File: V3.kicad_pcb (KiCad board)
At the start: 2 copper layers, 128.2 x 61 mm, 109 parts, among them IC1 TPS62840DLCR","TPS62840DLCR, J1 Conn_01x04, J2 Conn_01x04, J3 FFC2B28-24-G, J4 Conn_01x04, J6 Conn_01x02, J7 Conn_01x02, Q3 FDN304P","FDN304P, Q4 FDN304P","FDN304P, Q8 SI1308EDL","SI1308EDL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

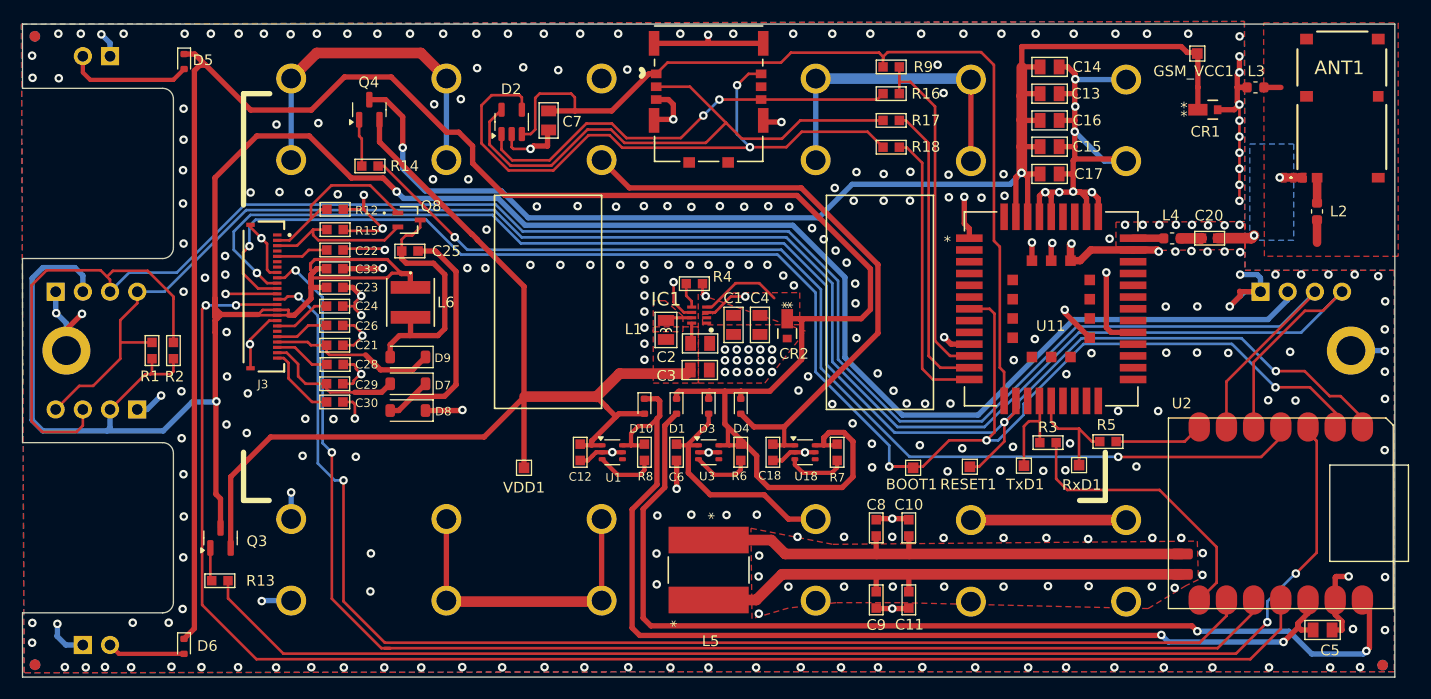
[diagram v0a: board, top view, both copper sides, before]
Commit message: edit fotprint of xiao module
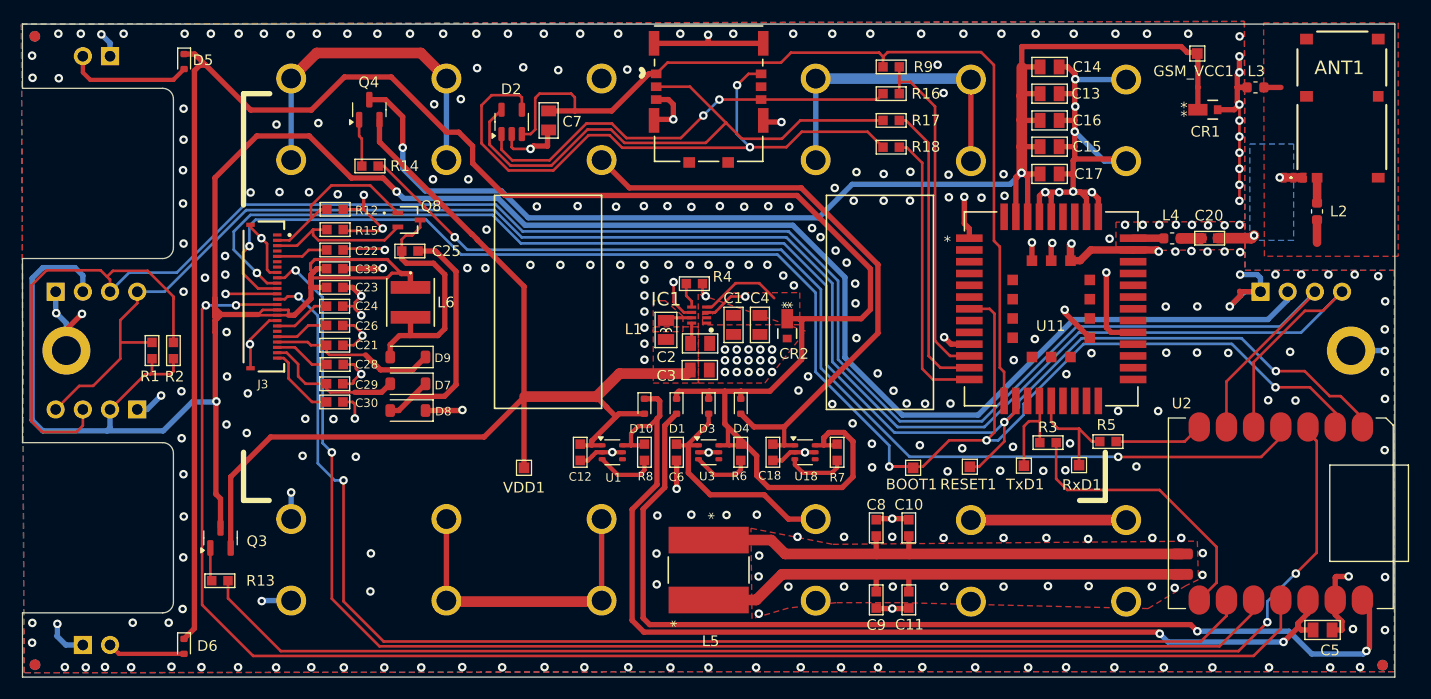
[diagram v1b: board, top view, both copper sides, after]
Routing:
- net DISPLAY_BUSY: track 124.6 -> 123.3 mm
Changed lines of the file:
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@@
 		)
 		(fp_line
+			(start 0 0)
+			(end 0 -1.6)
+			(stroke
+				(width 0.1)
+				(type default)
+			)
+			(layer "F.SilkS")
+		)
+		(fp_line
 			(start 17.8 0)
-			(end 17.8 -21)
+			(end 17.8 -1.6)
 			(stroke
-				(width 0.127)
-				(type solid)
+				(width 0.1)
+				(type default)
 			)
 			(layer "F.SilkS")
@@
 		(fp_line
 			(start 0 -20.3285)
-			(end 0 0)
+			(end 0 -19.4)
 			(stroke
-				(width 0.127)
-				(type solid)
+				(width 0.1)
+				(type default)
 			)
 			(layer "F.SilkS")
@@
 		(fp_line
 			(start 17.8 -21)
+			(end 17.8 -19.5)
+			(stroke
+				(width 0.1)
+				(type default)
+			)
+			(layer "F.SilkS")
+		)
+		(fp_line
+			(start 17.8 -21)
 			(end 0.671541 -21)
 			(stroke
@@
 	)
 	(segment
-		(start 53.45 25.98)
-		(end 53.45 24.2)
+		(start -47.32 -3.88)
+		(end -47.32 23.76)
 		(width 0.25)
 		(layer "F.Cu")
@@
 	)
 	(segment
-		(start -47.32 23.76)
-		(end -42.25 28.83)
+		(start -42.555 28.525)
+		(end 50.905 28.525)
 		(width 0.25)
 		(layer "F.Cu")
@@
 	)
 	(segment
-		(start 50.6 28.83)
-		(end 53.45 25.98)
+		(start 53.45 25.98)
+		(end 53.45 24.2)
 		(width 0.25)
 		(layer "F.Cu")
@@
 	)
 	(segment
-		(start -47.32 -3.88)
-		(end -47.32 23.76)
+		(start 50.905 28.525)
+		(end 53.45 25.98)
 		(width 0.25)
 		(layer "F.Cu")
@@
 	)
 	(segment
-		(start -42.25 28.83)
-		(end 50.6 28.83)
+		(start -47.32 23.76)
+		(end -42.555 28.525)
 		(width 0.25)
 		(layer "F.Cu")
@@
 	)
 	(segment
-		(start -44.9 23.14)
-		(end -44.9 21.5)
+		(start 49.495 28.075)
+		(end -39.965 28.075)
 		(width 0.25)
 		(layer "F.Cu")
@@
 	)
 	(segment
-		(start 49.26 28.31)
-		(end -39.73 28.31)
+		(start 52.19 25.37)
+		(end 52.19 25.38)
+		(width 0.25)
+		(layer "F.Cu")
+		(net 7)
+	)
+	(segment
+		(start -44.9 23.14)
+		(end -44.9 21.5)
 		(width 0.25)
 		(layer "F.Cu")
@@
 	)
 	(segment
-		(start -39.73 28.31)
-		(end -44.9 23.14)
+		(start 52.19 25.38)
+		(end 49.495 28.075)
 		(width 0.25)
 		(layer "F.Cu")
@@
 	)
 	(segment
-		(start 52.19 25.38)
-		(end 49.26 28.31)
-		(width 0.25)
-		(layer "F.Cu")
-		(net 7)
-	)
-	(segment
-		(start 52.19 25.37)
-		(end 52.19 25.38)
+		(start -39.965 28.075)
+		(end -44.9 23.14)
 		(width 0.25)
 		(layer "F.Cu")
@@
 	)
 	(segment
-		(start -4.83 12.52)
-		(end -4.83 6.37)
-		(width 0.5)
-		(layer "F.Cu")
-		(net 9)
-	)
-	(segment
-		(start -7.15 14.84)
-		(end -4.83 12.52)
-		(width 0.5)
-		(layer "F.Cu")
-		(net 9)
-	)
-	(segment
 		(start 56.461 26.1)
 		(end 55.35 26.1)
@@
 	)
 	(segment
-		(start -4.83 6.37)
-		(end -4.57 6.11)
-		(width 0.5)
-		(layer "F.Cu")
-		(net 9)
-	)
-	(segment
 		(start -7.25 7.74)
 		(end -6.56 7.05)
@@
 	)
 	(segment
+		(start 41.99 26.3)
+		(end 42.14 26.45)
+		(width 0.5)
+		(layer "F.Cu")
+		(net 9)
+	)
+	(segment
 		(start -4.78 4.5)
 		(end -6 4.5)
@@
 	)
 	(segment
-		(start 53.7 27.22)
-		(end 55.05 25.87)
+		(start -4.83 6.37)
+		(end -4.83 12.52)
 		(width 0.5)
 		(layer "F.Cu")
@@
 	)
 	(segment
-		(start -7.25 8.85)
-		(end -6.111999 8.85)
-		(width 0.4)
+		(start 53.7 27.22)
+		(end 55.05 25.87)
+		(width 0.5)
 		(layer "F.Cu")
 		(net 9)
 	)
 	(segment
-		(start -7.15 25.9)
-		(end -7.15 14.84)
+		(start -7.15 14.84)
+		(end -7.15 25.2)
 		(width 0.5)
 		(layer "F.Cu")
@@
 	)
 	(segment
-		(start 42.245 26.61)
-		(end -6.44 26.61)
+		(start -6.05 26.3)
+		(end 41.99 26.3)
 		(width 0.5)
 		(layer "F.Cu")
@@
 	)
 	(segment
-		(start 42.29 26.565)
-		(end 42.245 26.61)
-		(width 0.5)
+		(start -7.25 8.85)
+		(end -6.111999 8.85)
+		(width 0.4)
 		(layer "F.Cu")
 		(net 9)
@@
 	)
 	(segment
-		(start -6.44 26.61)
-		(end -7.15 25.9)
+		(start 55.05 25.47)
+		(end 55.99 24.53)
 		(width 0.5)
 		(layer "F.Cu")
@@
 	)
 	(segment
-		(start 55.05 25.47)
-		(end 55.99 24.53)
+		(start 55.05 25.87)
+		(end 55.05 25.8)
 		(width 0.5)
 		(layer "F.Cu")
@@
 	)
 	(segment
-		(start 55.05 25.87)
-		(end 55.05 25.8)
+		(start -4.57 6.11)
+		(end -4.83 6.37)
+		(width 0.5)
+		(layer "F.Cu")
+		(net 9)
+	)
+	(segment
+		(start -7.15 25.2)
+		(end -6.05 26.3)
+		(width 0.5)
+		(layer "F.Cu")
+		(net 9)
+	)
+	(segment
+		(start -4.83 12.52)
+		(end -7.15 14.84)
 		(width 0.5)
 		(layer "F.Cu")
@@
 	)
 	(via
-		(at 42.29 26.565)
+		(at 42.14 26.45)
 		(size 0.8)
 		(drill 0.4)
@@
 	)
 	(segment
-		(start 53.7 27.22)
-		(end 42.945 27.22)
+		(start 42.14 26.45)
+		(end 42.91 27.22)
 		(width 0.5)
 		(layer "B.Cu")
@@
 	)
 	(segment
-		(start 42.945 27.22)
-		(end 42.29 26.565)
+		(start 42.91 27.22)
+		(end 53.7 27.22)
 		(width 0.5)
 		(layer "B.Cu")
@@
 	)
 	(segment
-		(start 45.86 27.29)
-		(end -30.25 27.29)
-		(width 0.25)
-		(layer "F.Cu")
-		(net 12)
-	)
-	(segment
 		(start -38.31 -5.06)
 		(end -39.33 -5.06)
@@
 	(segment
 		(start 48.37 24.78)
-		(end 45.86 27.29)
+		(end 45.975 27.175)
 		(width 0.25)
 		(layer "F.Cu")
@@
 	)
 	(segment
-		(start -30.25 27.29)
-		(end -34.11 23.43)
+		(start 45.975 27.175)
+		(end -30.365 27.175)
 		(width 0.25)
 		(layer "F.Cu")
@@
 	)
 	(segment
+		(start -30.365 27.175)
+		(end -34.11 23.43)
+		(width 0.25)
+		(layer "F.Cu")
+		(net 12)
+	)
+	(segment
 		(start -39.59 -4.8)
 		(end -40.3 -4.8)
@@
 	)
 	(segment
-		(start -29.73 27.8)
-		(end -30.58 27.8)
+		(start -35.2 23.18)
+		(end -30.755 27.625)
 		(width 0.25)
 		(layer "F.Cu")
@@
 	)
 	(segment
-		(start -35.2 23.18)
-		(end -30.58 27.8)
+		(start -38.91 -7.49)
+		(end -39.600001 -6.799999)
 		(width 0.25)
 		(layer "F.Cu")
@@
 	)
 	(segment
-		(start -38.91 -7.49)
-		(end -39.600001 -6.799999)
+		(start 47.725 27.625)
+		(end 50.91 24.44)
 		(width 0.25)
 		(layer "F.Cu")
@@
 	)
 	(segment
-		(start -35.2 9.51)
-		(end -35.2 23.18)
-		(width 0.25)
-		(layer "F.Cu")
-		(net 74)
-	)
-	(segment
-		(start -30.28 27.8)
-		(end 47.55 27.8)
+		(start -30.755 27.625)
+		(end 47.725 27.625)
 		(width 0.25)
 		(layer "F.Cu")
@@
 	)
 	(segment
-		(start 47.55 27.8)
-		(end 50.91 24.44)
-		(width 0.25)
-		(layer "F.Cu")
-		(net 74)
-	)
-	(segment
-		(start -30.28 27.8)
-		(end -29.73 27.8)
+		(start -35.2 9.51)
+		(end -35.2 23.18)
 		(width 0.25)
 		(layer "F.Cu")
@@
 	)
 	(via
-		(at 10.75 -10.4)
+		(at 10.45 -10.6)
 		(size 0.8)
 		(drill 0.4)
@@
 	)
 	(segment
-		(start -6.12 14.79995)
-		(end -4.1 12.77995)
+		(start -4.1 12.77995)
+		(end -4.1 7)
 		(width 0.5)
 		(layer "F.Cu")
@@
 	)
 	(segment
-		(start -4.1 12.77995)
-		(end -4.1 7)
+		(start -6.12 24.99)
+		(end -6.12 14.79995)
 		(width 0.5)
 		(layer "F.Cu")
@@
 	)
 	(segment
-		(start -5.395 25.715)
-		(end -6.12 24.99)
+		(start 45.65 26.22)
+		(end 45.03 25.6)
 		(width 0.5)
 		(layer "F.Cu")
@@
 	)
 	(segment
-		(start -6.12 24.99)
-		(end -6.12 14.79995)
+		(start -5.51 25.6)
+		(end -6.12 24.99)
 		(width 0.5)
 		(layer "F.Cu")
@@
 	)
 	(segment
-		(start 45.145 25.715)
-		(end -5.395 25.715)
+		(start -4.1 7)
+		(end -3 5.9)
 		(width 0.5)
 		(layer "F.Cu")
@@
 	)
 	(segment
-		(start 45.65 26.22)
-		(end 45.145 25.715)
+		(start 45.03 25.6)
+		(end -5.51 25.6)
 		(width 0.5)
 		(layer "F.Cu")
@@
 	)
 	(segment
-		(start 61.73 24.22)
-		(end 60.94 23.43)
+		(start -6.12 14.79995)
+		(end -4.1 12.77995)
 		(width 0.5)
 		(layer "F.Cu")
@@
 	)
 	(segment
-		(start -4.1 7)
-		(end -3 5.9)
+		(start 61.73 24.22)
+		(end 60.94 23.43)
 		(width 0.5)
 		(layer "F.Cu")

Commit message: order submitted
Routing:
- net DISPLAY_SCK: track 119.3 -> 120.8 mm
- net +BATT: track 201.6 -> 202.3 mm
- net GND: vias 331 -> 336
